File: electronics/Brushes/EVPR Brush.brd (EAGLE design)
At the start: 64.8 x 11.8 mm, 0 parts

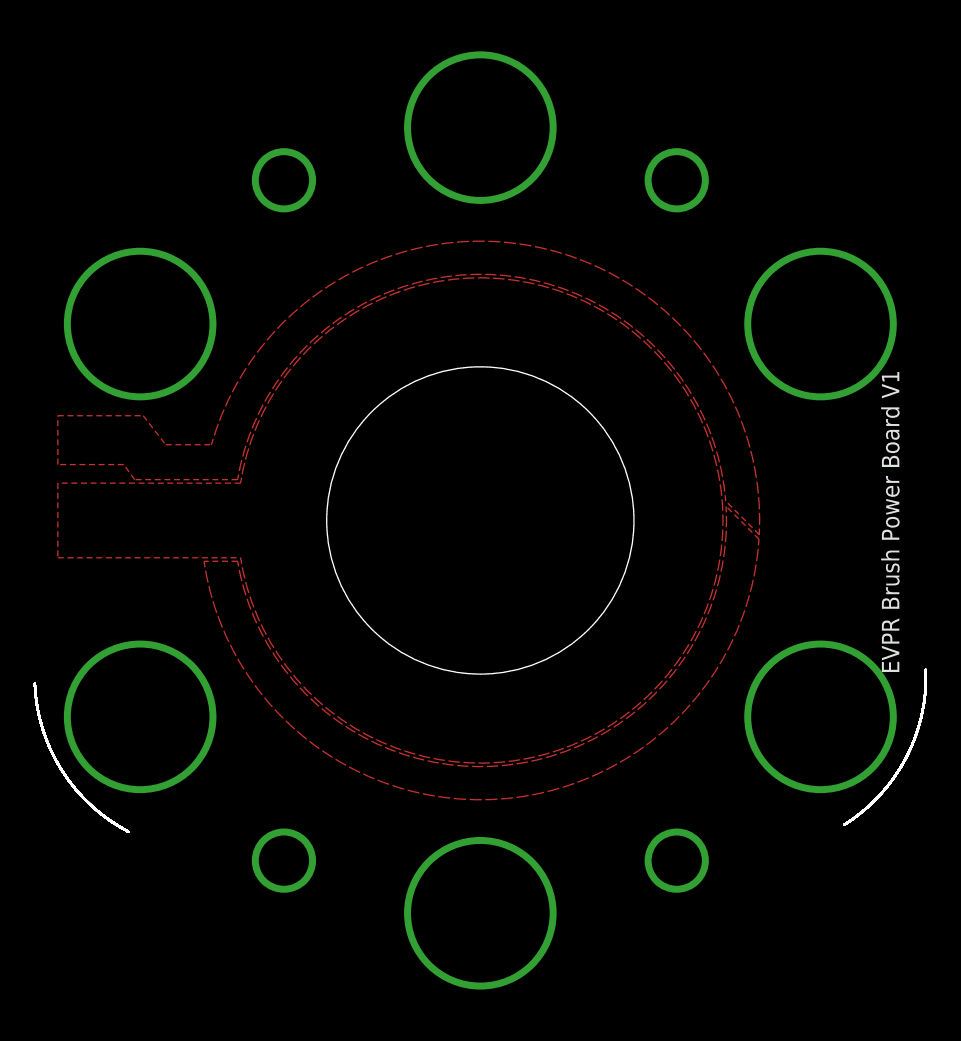
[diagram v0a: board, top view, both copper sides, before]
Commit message: Add paste to BOM, brush plate updates.
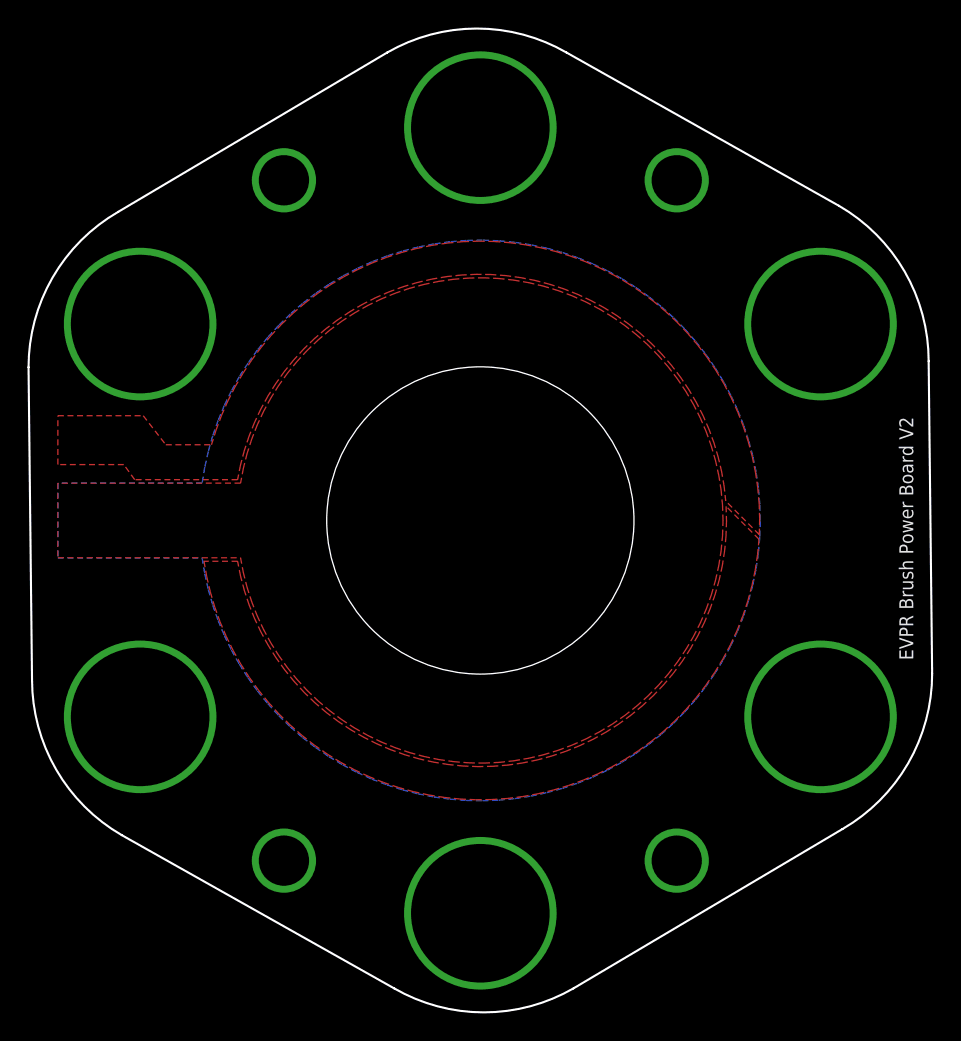
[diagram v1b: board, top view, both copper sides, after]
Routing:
- added copper zone on layer 16, net POWER
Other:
- board size 64.8 x 11.8 mm -> 65.7 x 71.6 mm
- board text added: "EVPR Brush Power Board V2"
- board text removed: "EVPR Brush Power Board V1"
